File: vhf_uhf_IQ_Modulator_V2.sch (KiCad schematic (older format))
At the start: 72 parts, among them J1 Conn_01x06, J2 TEST_1P, J3 Audio-Jack-3, J4 CONN_01X04, J5 SMA Edge FM, Q1 BC817-40, Q2 BC817-40, Q3 BC817-40, U1 TRF3701, U2 MMZ09332BT1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

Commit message: Trying to fic U3 Footprint
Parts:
- removed J1: Conn_01x06, Connectors_Molex:Molex_KK-6410-06_06x2.54mm_Straight, symbol Conn_01x06
- removed U?: Si570, Oscillators:Oscillator_SI570_SI571_Standard, symbol si570
- added J1: CONN_01X03, Pin_Headers:Pin_Header_Straight_1x03_Pitch2.54mm, symbol CONN_01X03
- J2: footprint Inductors_SMD:L_0805_HandSoldering -> Pin_Headers:Pin_Header_Straight_1x01_Pitch2.54mm
- J3: footprint Connectors_Molex:Molex_KK-6410-03_03x2.54mm_Straight -> Pin_Headers:Pin_Header_Straight_1x03_Pitch2.54mm
- J4: footprint Connectors_Molex:Molex_KK-6410-04_04x2.54mm_Straight -> Pin_Headers:Pin_Header_Straight_1x04_Pitch2.54mm
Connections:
- net labels removed: INT
- wire segments 216 -> 215
- no-connect marks 16 -> 17

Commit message: Added printable Diagram
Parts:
- RV1, RV2: footprint Resistors_SMD:R_0805_HandSoldering -> Potentiometer_SMD:Potentiometer_Bourns_3314G_Vertical
- U2: footprint Resistors_SMD:R_0805_HandSoldering -> QFN-12-1EP_3x3mm:QFN-12-1EP_3x3mm_P0.5mm_EP1.65x1.65mm
- U3: footprint Oscillators:Oscillator_SI570_SI571_Standard -> Oscillators:Oscillator_SMD_SI570_SI571_HandSoldering
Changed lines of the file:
@@
 F 0 "RV2" V 9775 1150 50  0000 C CNN
 F 1 "4k7" V 9850 1150 50  0000 C CNN
-F 2 "Resistors_SMD:R_0805_HandSoldering" H 9950 1150 50  0001 C CNN
+F 2 "Potentiometer_SMD:Potentiometer_Bourns_3314G_Vertical" H 9950 1150 50  0001 C CNN
 F 3 "" H 9950 1150 50  0001 C CNN
 	1    9950 1150
@@
 F 0 "RV1" V 9025 1150 50  0000 C CNN
 F 1 "4k7" V 9100 1150 50  0000 C CNN
-F 2 "Resistors_SMD:R_0805_HandSoldering" H 9200 1150 50  0001 C CNN
+F 2 "Potentiometer_SMD:Potentiometer_Bourns_3314G_Vertical" H 9200 1150 50  0001 C CNN
 F 3 "" H 9200 1150 50  0001 C CNN
 	1    9200 1150
@@
 F 0 "U2" H 13050 3700 60  0000 C CNN
 F 1 "MMZ09332BT1" H 12350 2250 60  0000 C CNN
-F 2 "Resistors_SMD:R_0805_HandSoldering" H 12850 3000 60  0001 C CNN
+F 2 "QFN-12-1EP_3x3mm:QFN-12-1EP_3x3mm_P0.5mm_EP1.65x1.65mm" H 12850 3000 60  0001 C CNN
 F 3 "" H 12850 3000 60  0001 C CNN
 	1    12850 3000
@@
 F 0 "U3" H 6950 4350 50  0000 C CNN
 F 1 "Si570" H 7700 3550 50  0000 C CNN
-F 2 "Oscillators:Oscillator_SI570_SI571_Standard" H 6800 4550 50  0001 C CNN
+F 2 "Oscillators:Oscillator_SMD_SI570_SI571_HandSoldering" H 6800 4550 50  0001 C CNN
 F 3 "" H 6950 4650 50  0001 C CNN
 	1    7350 3950

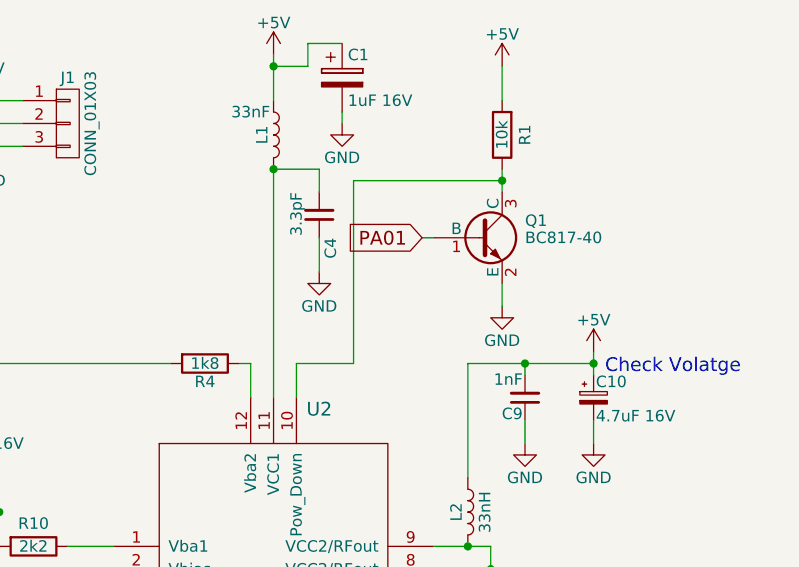
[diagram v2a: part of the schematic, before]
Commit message: Found library error
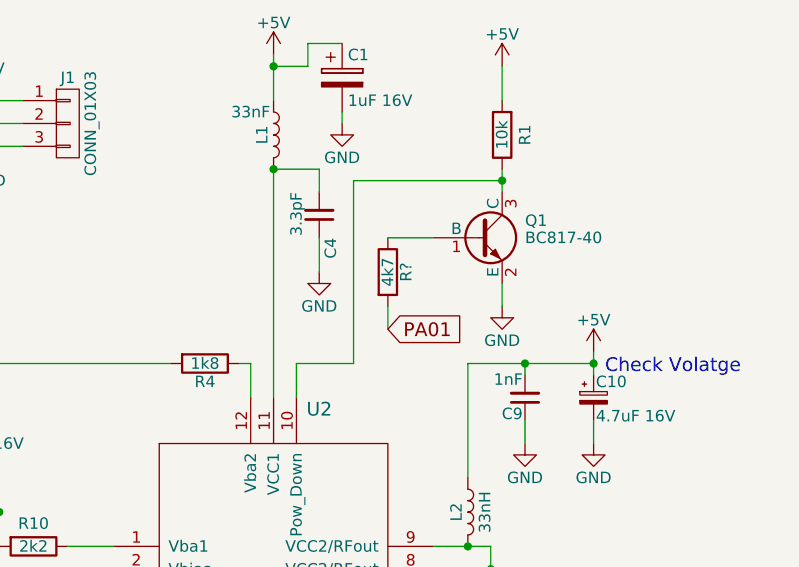
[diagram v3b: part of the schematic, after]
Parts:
- added R?: 4k7, symbol R
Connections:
- net PA01: now also R?.2; no longer Q1.1 (B)
- new net: Q1.1 (B), R?.1
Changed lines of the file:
@@
 Text GLabel 8250 5350 2    60   Input ~ 0
 PDet
-Text GLabel 13500 1550 0    60   Input ~ 0
+Text GLabel 13350 1950 2    60   Input ~ 0
 PA01
 Wire Wire Line
-	13500 1550 13550 1550
+	13350 1550 13550 1550
 NoConn ~ 5700 5900
 Text GLabel 13100 3800 2    60   Output ~ 0
@@
 Wire Wire Line
 	3250 3150 3600 3150
+$Comp
+L R R?
+U 1 1 5B1F16F5
+P 13350 1700
+F 0 "R?" V 13430 1700 50  0000 C CNN
+F 1 "4k7" V 13350 1700 50  0000 C CNN
+F 2 "" V 13280 1700 50  0001 C CNN
+F 3 "" H 13350 1700 50  0001 C CNN
+	1    13350 1700
+	1    0    0    -1
+$EndComp
+Wire Wire Line
+	13350 1850 13350 1950
 $EndSCHEMATC
